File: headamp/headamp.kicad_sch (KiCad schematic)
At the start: 91 parts, among them J1 MAINS 230V, J401 IN L (RCA), J402 IN R (RCA), J403 jack 6,3mm TRS (DT 770 M 80R), K1 9V, SW1 ON/OFF, SW2 S2 wokal, SW202 S2 wokal (P), SW401 S1 crossfeed, T1 OPT SE 5k:80R (>=25H, 45mA), T201 OPT SE 5k:80R (>=25H, 45mA), T301 EI84 100VA: 230V : 250V/0,15A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, U1 ECC82, U2 EL84 (trioda), U202 EL84 (trioda), U301 LD1085 (LDO)

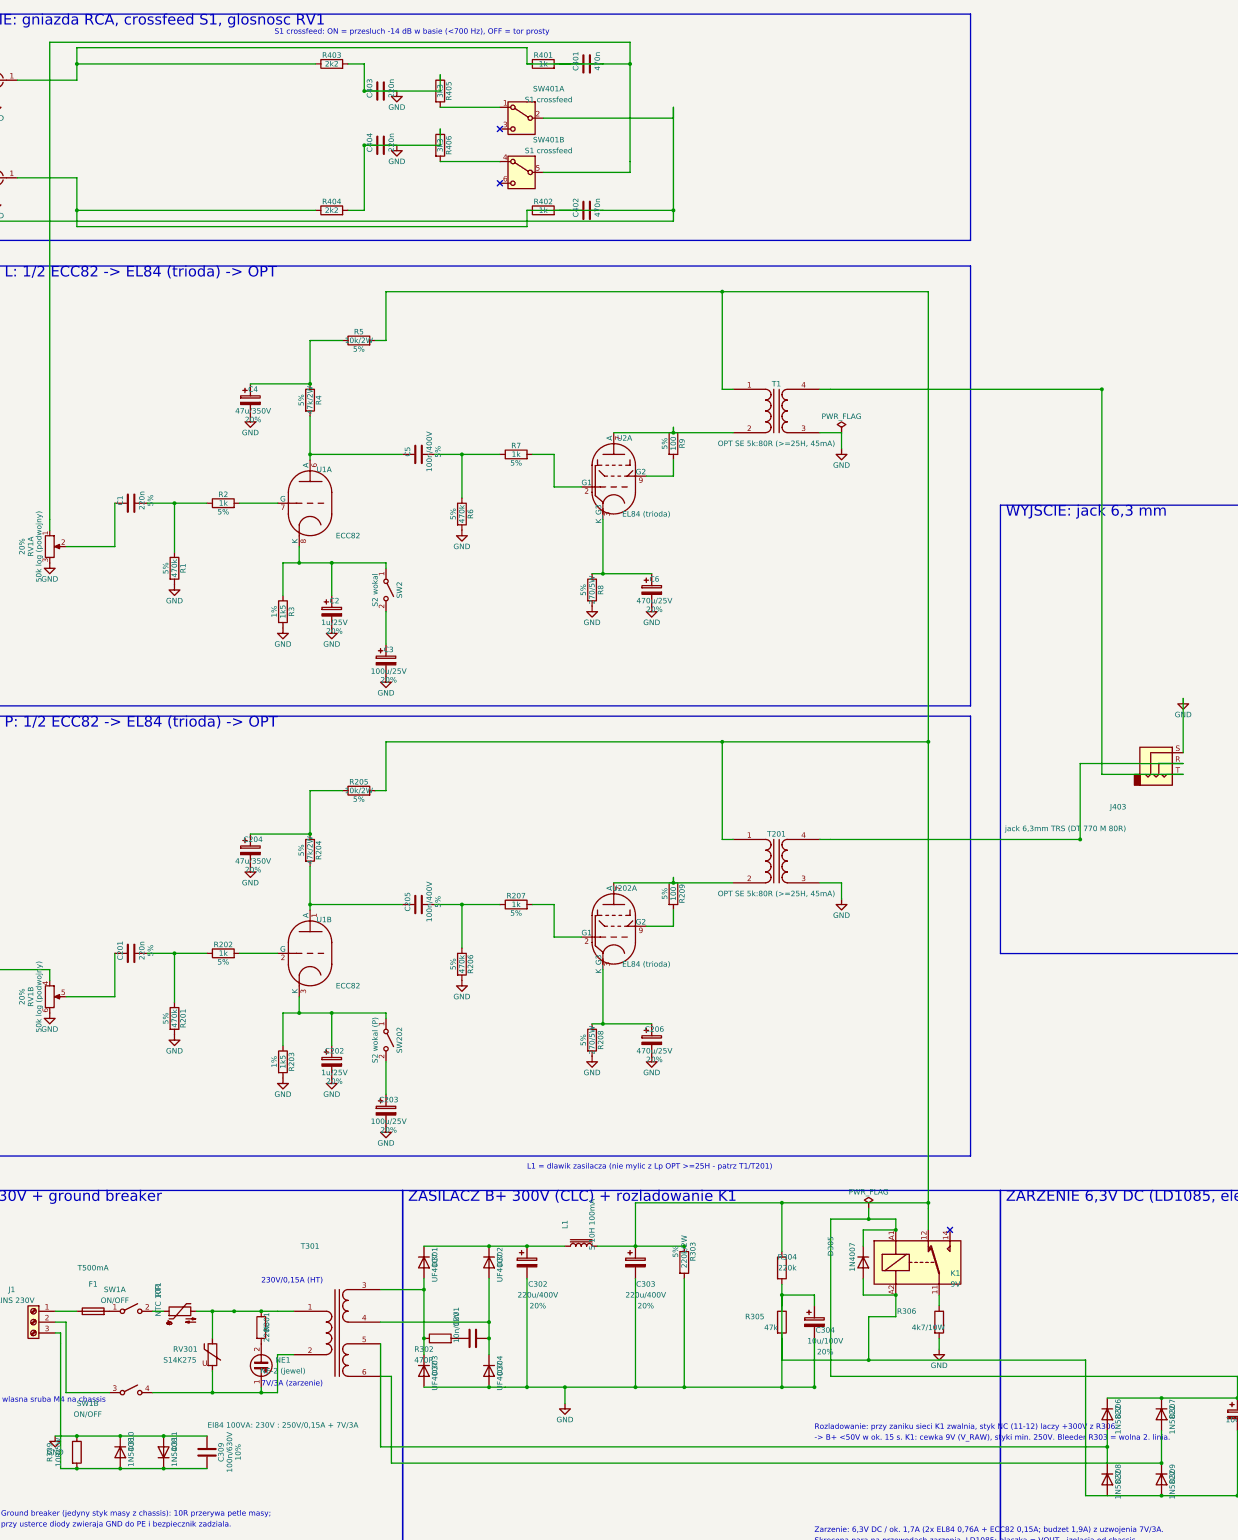
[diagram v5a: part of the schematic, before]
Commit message: headamp: gen.py - brak nakladajacych sie drutow (Eeschema scalalo je i gubilo polaczenia), test geometrii w check.py
Eeschema (KiCad 10.0.6) przy zapisie scala wspolliniowe odcinki drutu
stykajace sie koncami bez pinu/junction/trzeciego drutu. gen.py emitowal
kilka miejsc z nakladajacymi sie wspolliniowymi odcinkami (albo odcinkiem
przechodzacym przez pin/koniec innego drutu bez junction), co
kicad-cli erc/netlist nie widzi (0/0, netlista poprawna), ale po otwarciu
i zapisaniu w Eeschema dawalo 7 pin_not_connected + 3
unconnected_wire_endpoint.

- headamp/check_geom.py (nowy): test geometrii .kicad_sch - brak
  nakladajacych sie odcinkow, brak przejscia przez pin/koniec drutu bez
  junction, brak odcinkow < 1.27mm, brak dyndajacych koncow, oraz emulacja
  scalania kolinearnych drutow przez Eeschema + porownanie wynikowej
  partycji pinow z prawdziwa netlista kicad-cli (test regresji). Wywolywany
  automatycznie z check.py.
- headamp/gen.py: naprawiony routing w 7 miejscach (tor prosty R401-R406,
  magistrala SW401 outR, wezel elewacji R304/R305, mostek zarzenia T301) -
  wszedzie jog omijajacy kolizje zamiast prostej linii przez pin/koniec.
  xform() przeniesiony do symlib.py (dzielony z check_geom.py).
- docs/PROJEKT-HEADAMP.md, CLAUDE.md: notka o teście geometrii.

Weryfikacja: check_geom.py OK (emulacja scalania = netlista kicad-cli),
check.py OK (58 siec, te same asercje), ERC 0/0, gen.py idempotentny.

Co-Authored-By: Claude Sonnet 5 <noreply@anthropic.com>
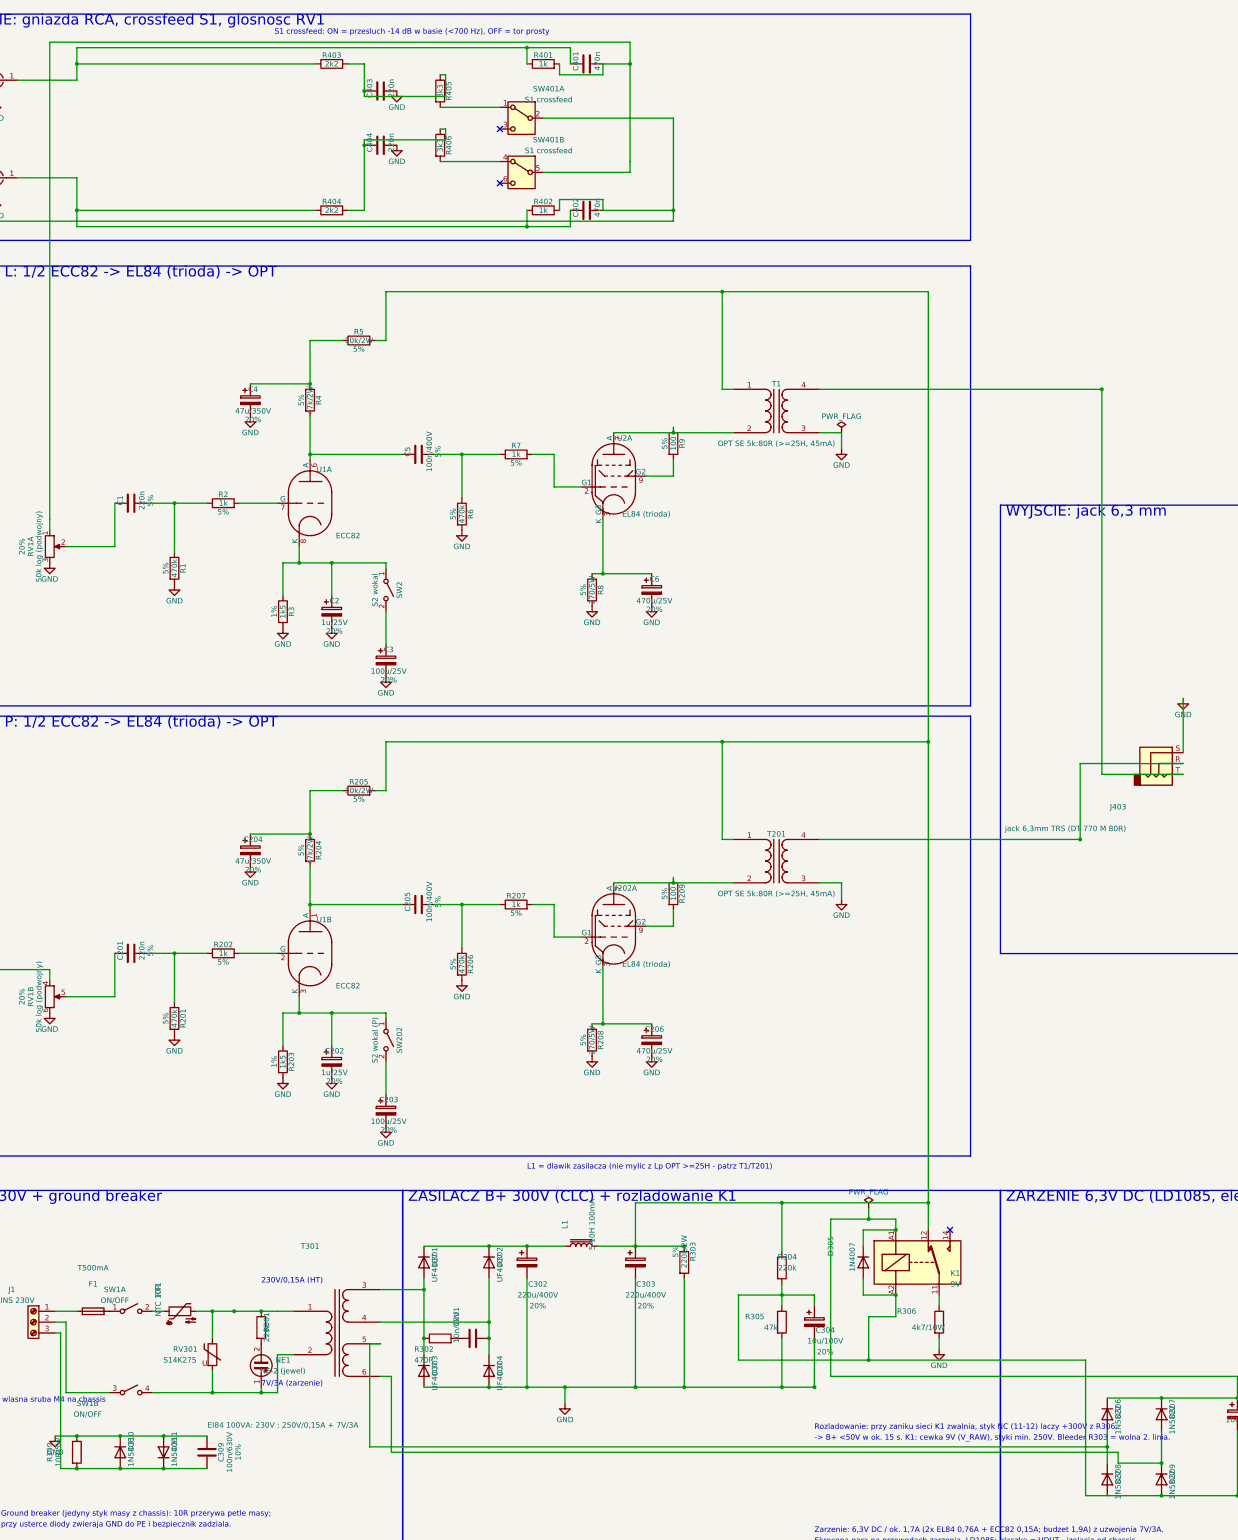
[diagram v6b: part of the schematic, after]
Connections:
- net GND: no longer C304.1, C305.2, C306.2, C307.2, C308.2, D305.2 (A), D308.2 (A), D309.2 (A), K1.A2, R304.2, R305.1, R308.2, U1.9 (F2), U2.5 (F2), U202.5 (F2)
- net at C402.2, R402.2, RV1.4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: no longer C402.1, J402.1 (In), R402.1, R404.1
- net at C401.2, R401.2, RV1.1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: no longer C401.1, J401.1 (In), R401.1, R403.1
- new net: C304.1, C305.2, C306.2, C307.2, C308.2, D305.2 (A), D308.2 (A), D309.2 (A), K1.A2, R304.2, R305.1, R308.2, U1.9 (F2), U2.5 (F2), U202.5 (F2)
- new net: C401.1, J401.1 (In), R401.1, R403.1
- new net: C402.1, J402.1 (In), R402.1, R404.1
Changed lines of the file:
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@@
   (junction (at 185.42 218.44) (diameter 0))
   (junction (at 196.85 185.42) (diameter 0))
+  (junction (at 151.13 22.86) (diameter 0))
   (junction (at 45.72 26.67) (diameter 0))
+  (junction (at 151.13 64.77) (diameter 0))
   (junction (at 45.72 60.96) (diameter 0))
   (junction (at 175.26 26.67) (diameter 0))
@@
   (wire (pts (xy 45.72 26.67) (xy 101.6 26.67)) (stroke (width 0) (type default)))
   (wire (pts (xy 45.72 26.67) (xy 45.72 22.86)) (stroke (width 0) (type default)))
-  (wire (pts (xy 45.72 22.86) (xy 151.13 22.86)) (stroke (width 0) (type default)))
+  (wire (pts (xy 45.72 22.86) (xy 161.29 22.86)) (stroke (width 0) (type default)))
   (wire (pts (xy 151.13 22.86) (xy 151.13 26.67)) (stroke (width 0) (type default)))
+  (wire (pts (xy 161.29 22.86) (xy 161.29 26.67)) (stroke (width 0) (type default)))
   (wire (pts (xy 31.75 53.34) (xy 45.72 53.34)) (stroke (width 0) (type default)))
   (wire (pts (xy 45.72 53.34) (xy 45.72 60.96)) (stroke (width 0) (type default)))
   (wire (pts (xy 45.72 60.96) (xy 101.6 60.96)) (stroke (width 0) (type default)))
   (wire (pts (xy 45.72 60.96) (xy 45.72 64.77)) (stroke (width 0) (type default)))
-  (wire (pts (xy 45.72 64.77) (xy 151.13 64.77)) (stroke (width 0) (type default)))
+  (wire (pts (xy 45.72 64.77) (xy 161.29 64.77)) (stroke (width 0) (type default)))
   (wire (pts (xy 151.13 64.77) (xy 151.13 60.96)) (stroke (width 0) (type default)))
-  (wire (pts (xy 151.13 26.67) (xy 161.29 26.67)) (stroke (width 0) (type default)))
-  (wire (pts (xy 158.75 26.67) (xy 168.91 26.67)) (stroke (width 0) (type default)))
-  (wire (pts (xy 151.13 60.96) (xy 161.29 60.96)) (stroke (width 0) (type default)))
-  (wire (pts (xy 158.75 60.96) (xy 168.91 60.96)) (stroke (width 0) (type default)))
+  (wire (pts (xy 161.29 64.77) (xy 161.29 60.96)) (stroke (width 0) (type default)))
+  (wire (pts (xy 158.75 26.67) (xy 158.75 29.21)) (stroke (width 0) (type default)))
+  (wire (pts (xy 158.75 29.21) (xy 168.91 29.21)) (stroke (width 0) (type default)))
+  (wire (pts (xy 168.91 29.21) (xy 168.91 26.67)) (stroke (width 0) (type default)))
+  (wire (pts (xy 158.75 60.96) (xy 158.75 58.42)) (stroke (width 0) (type default)))
+  (wire (pts (xy 158.75 58.42) (xy 168.91 58.42)) (stroke (width 0) (type default)))
+  (wire (pts (xy 168.91 58.42) (xy 168.91 60.96)) (stroke (width 0) (type default)))
   (wire (pts (xy 168.91 26.67) (xy 175.26 26.67)) (stroke (width 0) (type default)))
   (wire (pts (xy 175.26 21.59) (xy 175.26 49.53)) (stroke (width 0) (type default)))
@@
   (wire (pts (xy 39.37 21.59) (xy 39.37 133.35)) (stroke (width 0) (type default)))
   (wire (pts (xy 168.91 60.96) (xy 185.42 60.96)) (stroke (width 0) (type default)))
-  (wire (pts (xy 185.42 36.83) (xy 185.42 63.5)) (stroke (width 0) (type default)))
+  (wire (pts (xy 185.42 39.37) (xy 185.42 63.5)) (stroke (width 0) (type default)))
   (wire (pts (xy 185.42 63.5) (xy 20.32 63.5)) (stroke (width 0) (type default)))
   (wire (pts (xy 20.32 63.5) (xy 20.32 238.76)) (stroke (width 0) (type default)))
@@
   (wire (pts (xy 109.22 26.67) (xy 113.03 26.67)) (stroke (width 0) (type default)))
   (wire (pts (xy 113.03 26.67) (xy 113.03 33.02)) (stroke (width 0) (type default)))
-  (wire (pts (xy 113.03 33.02) (xy 130.81 33.02)) (stroke (width 0) (type default)))
-  (wire (pts (xy 130.81 33.02) (xy 130.81 29.21)) (stroke (width 0) (type default)))
+  (wire (pts (xy 113.03 33.02) (xy 113.03 34.29)) (stroke (width 0) (type default)))
+  (wire (pts (xy 113.03 34.29) (xy 132.08 34.29)) (stroke (width 0) (type default)))
+  (wire (pts (xy 132.08 34.29) (xy 132.08 29.21)) (stroke (width 0) (type default)))
+  (wire (pts (xy 132.08 29.21) (xy 130.81 29.21)) (stroke (width 0) (type default)))
   (wire (pts (xy 130.81 36.83) (xy 144.78 36.83)) (stroke (width 0) (type default)))
   (wire (pts (xy 154.94 39.37) (xy 185.42 39.37)) (stroke (width 0) (type default)))
-  (wire (pts (xy 185.42 39.37) (xy 185.42 36.83)) (stroke (width 0) (type default)))
   (wire (pts (xy 109.22 60.96) (xy 113.03 60.96)) (stroke (width 0) (type default)))
   (wire (pts (xy 113.03 60.96) (xy 113.03 45.72)) (stroke (width 0) (type default)))
-  (wire (pts (xy 113.03 45.72) (xy 130.81 45.72)) (stroke (width 0) (type default)))
-  (wire (pts (xy 130.81 45.72) (xy 130.81 41.91)) (stroke (width 0) (type default)))
+  (wire (pts (xy 113.03 45.72) (xy 113.03 44.45)) (stroke (width 0) (type default)))
+  (wire (pts (xy 113.03 44.45) (xy 132.08 44.45)) (stroke (width 0) (type default)))
+  (wire (pts (xy 132.08 44.45) (xy 132.08 41.91)) (stroke (width 0) (type default)))
+  (wire (pts (xy 132.08 41.91) (xy 130.81 41.91)) (stroke (width 0) (type default)))
   (wire (pts (xy 130.81 49.53) (xy 144.78 49.53)) (stroke (width 0) (type default)))
   (wire (pts (xy 154.94 52.07) (xy 175.26 52.07)) (stroke (width 0) (type default)))
@@
   (wire (pts (xy 245.11 185.42) (xy 245.11 293.37)) (stroke (width 0) (type default)))
   (wire (pts (xy 287.02 346.71) (xy 287.02 354.33)) (stroke (width 0) (type default)))
-  (wire (pts (xy 116.84 326.39) (xy 116.84 350.52)) (stroke (width 0) (type default)))
-  (wire (pts (xy 116.84 350.52) (xy 287.02 350.52)) (stroke (width 0) (type default)))
+  (wire (pts (xy 116.84 326.39) (xy 114.3 326.39)) (stroke (width 0) (type default)))
+  (wire (pts (xy 114.3 326.39) (xy 114.3 350.52)) (stroke (width 0) (type default)))
+  (wire (pts (xy 114.3 350.52) (xy 287.02 350.52)) (stroke (width 0) (type default)))
   (wire (pts (xy 299.72 346.71) (xy 299.72 354.33)) (stroke (width 0) (type default)))
   (wire (pts (xy 116.84 334.01) (xy 119.38 334.01)) (stroke (width 0) (type default)))
-  (wire (pts (xy 119.38 334.01) (xy 119.38 354.33)) (stroke (width 0) (type default)))
-  (wire (pts (xy 119.38 354.33) (xy 299.72 354.33)) (stroke (width 0) (type default)))
+  (wire (pts (xy 119.38 334.01) (xy 119.38 351.79)) (stroke (width 0) (type default)))
+  (wire (pts (xy 119.38 351.79) (xy 289.56 351.79)) (stroke (width 0) (type default)))
+  (wire (pts (xy 289.56 351.79) (xy 289.56 354.33)) (stroke (width 0) (type default)))
+  (wire (pts (xy 289.56 354.33) (xy 299.72 354.33)) (stroke (width 0) (type default)))
   (wire (pts (xy 287.02 339.09) (xy 299.72 339.09)) (stroke (width 0) (type default)))
   (wire (pts (xy 299.72 339.09) (xy 317.5 339.09)) (stroke (width 0) (type default)))
@@
   (wire (pts (xy 287.02 361.95) (xy 281.94 361.95)) (stroke (width 0) (type default)))
   (wire (pts (xy 387.35 361.95) (xy 387.35 364.49)) (stroke (width 0) (type default)))
-  (wire (pts (xy 210.82 314.96) (xy 210.82 330.2)) (stroke (width 0) (type default)))
-  (wire (pts (xy 210.82 330.2) (xy 231.14 330.2)) (stroke (width 0) (type default)))
+  (wire (pts (xy 210.82 314.96) (xy 200.66 314.96)) (stroke (width 0) (type default)))
+  (wire (pts (xy 200.66 314.96) (xy 200.66 330.2)) (stroke (width 0) (type default)))
+  (wire (pts (xy 200.66 330.2) (xy 231.14 330.2)) (stroke (width 0) (type default)))
   (wire (pts (xy 231.14 320.04) (xy 231.14 330.2)) (stroke (width 0) (type default)))
   (wire (pts (xy 231.14 330.2) (xy 281.94 330.2)) (stroke (width 0) (type default)))
